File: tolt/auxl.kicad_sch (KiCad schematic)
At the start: 8 parts, among them U17 BMI160, U18 ESP32-C3_SUPERMINI_SMD

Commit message: modified:   tolt/auxl.kicad_sch 	modified:   tolt/converters.kicad_sch 	modified:   tolt/tolt.kicad_pcb
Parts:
- added C144: 100n, Capacitor_SMD:C_0402_1005Metric, symbol Device:C
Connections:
- net GND: now also C144.1
- net VCC: no longer U17.8 (VDD)
- new net VDDA: C144.2, U17.8 (VDD)
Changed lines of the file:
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@@
 	(wire
 		(pts
-			(xy 67.564 66.548) (xy 67.564 68.326)
+			(xy 67.564 66.04) (xy 67.564 68.326)
 		)
 		(stroke
@@
 	)
 	(symbol
+		(lib_id "power:VDDA")
+		(at 67.564 66.04 0)
+		(unit 1)
+		(exclude_from_sim no)
+		(in_bom yes)
+		(on_board yes)
+		(dnp no)
+		(fields_autoplaced yes)
+		(property "Reference" "#PWR057"
+			(at 67.564 69.85 0)
+			(effects
+				(font
+					(size 1.27 1.27)
+				)
+				(hide yes)
+			)
+		)
+		(property "Value" "VDDA"
+			(at 67.564 61.214 0)
+			(effects
+				(font
+					(size 1.27 1.27)
+				)
+			)
+		)
+		(property "Footprint" ""
+			(at 67.564 66.04 0)
+			(effects
+				(font
+					(size 1.27 1.27)
+				)
+				(hide yes)
+			)
+		)
+		(property "Datasheet" ""
+			(at 67.564 66.04 0)
+			(effects
+				(font
+					(size 1.27 1.27)
+				)
+				(hide yes)
+			)
+		)
+		(property "Description" ""
+			(at 67.564 66.04 0)
+			(effects
+				(font
+					(size 1.27 1.27)
+				)
+				(hide yes)
+			)
+		)
+		(pin "1"
+		)
+		(instances
+			(project "tolt"
+				(path "/38c63d96-01d7-4159-b7c0-aa8cee77c3e9/5e8c7753-d04d-42ed-8285-d224e0d20653"
+					(reference "#PWR057")
+					(unit 1)
+				)
+			)
+		)
+	)
+	(symbol
 		(lib_id "Device:C")
 		(at 57.404 32.258 180)
@@
 	)
 	(symbol
+		(lib_id "Device:C")
+		(at 69.342 32.004 180)
+		(unit 1)
+		(exclude_from_sim no)
+		(in_bom yes)
+		(on_board yes)
+		(dnp no)
+		(fields_autoplaced yes)
+		(property "Reference" "C144"
+			(at 72.644 30.734 0)
+			(effects
+				(font
+					(size 1.27 1.27)
+				)
+				(justify right)
+			)
+		)
+		(property "Value" "100n"
+			(at 72.644 33.274 0)
+			(effects
+				(font
+					(size 1.27 1.27)
+				)
+				(justify right)
+			)
+		)
+		(property "Footprint" "Capacitor_SMD:C_0402_1005Metric"
+			(at 68.3768 28.194 0)
+			(effects
+				(font
+					(size 1.27 1.27)
+				)
+				(hide yes)
+			)
+		)
+		(property "Datasheet" "~"
+			(at 69.342 32.004 0)
+			(effects
+				(font
+					(size 1.27 1.27)
+				)
+				(hide yes)
+			)
+		)
+		(property "Description" ""
+			(at 69.342 32.004 0)
+			(effects
+				(font
+					(size 1.27 1.27)
+				)
+				(hide yes)
+			)
+		)
+		(pin "1"
+		)
+		(pin "2"
+		)
+		(instances
+			(project "tolt"
+				(path "/38c63d96-01d7-4159-b7c0-aa8cee77c3e9/5e8c7753-d04d-42ed-8285-d224e0d20653"
+					(reference "C144")
+					(unit 1)
+				)
+			)
+		)
+	)
+	(symbol
 		(lib_id "power:VCC")
 		(at 65.024 68.326 0)
@@
 	)
 	(symbol
+		(lib_id "power:VDDA")
+		(at 69.342 28.194 0)
+		(unit 1)
+		(exclude_from_sim no)
+		(in_bom yes)
+		(on_board yes)
+		(dnp no)
+		(fields_autoplaced yes)
+		(property "Reference" "#PWR062"
+			(at 69.342 32.004 0)
+			(effects
+				(font
+					(size 1.27 1.27)
+				)
+				(hide yes)
+			)
+		)
+		(property "Value" "VDDA"
+			(at 69.342 23.368 0)
+			(effects
+				(font
+					(size 1.27 1.27)
+				)
+			)
+		)
+		(property "Footprint" ""
+			(at 69.342 28.194 0)
+			(effects
+				(font
+					(size 1.27 1.27)
+				)
+				(hide yes)
+			)
+		)
+		(property "Datasheet" ""
+			(at 69.342 28.194 0)
+			(effects
+				(font
+					(size 1.27 1.27)
+				)
+				(hide yes)
+			)
+		)
+		(property "Description" ""
+			(at 69.342 28.194 0)
+			(effects
+				(font
+					(size 1.27 1.27)
+				)
+				(hide yes)
+			)
+		)
+		(pin "1"
+		)
+		(instances
+			(project "tolt"
+				(path "/38c63d96-01d7-4159-b7c0-aa8cee77c3e9/5e8c7753-d04d-42ed-8285-d224e0d20653"
+					(reference "#PWR062")
+					(unit 1)
+				)
+			)
+		)
+	)
+	(symbol
 		(lib_id "power:VCC")
 		(at 47.498 70.866 0)
@@
 	(symbol
 		(lib_id "power:VCC")
-		(at 67.564 66.548 0)
-		(unit 1)
-		(exclude_from_sim no)
-		(in_bom yes)
-		(on_board yes)
-		(dnp no)
-		(fields_autoplaced yes)
-		(property "Reference" "#PWR0172"
-			(at 67.564 70.358 0)
-			(effects
-				(font
-					(size 1.27 1.27)
-				)
-				(hide yes)
-			)
-		)
-		(property "Value" "VCC"
-			(at 67.564 61.468 0)
-			(effects
-				(font
-					(size 1.27 1.27)
-				)
-			)
-		)
-		(property "Footprint" ""
-			(at 67.564 66.548 0)
-			(effects
-				(font
-					(size 1.27 1.27)
-				)
-				(hide yes)
-			)
-		)
-		(property "Datasheet" ""
-			(at 67.564 66.548 0)
-			(effects
-				(font
-					(size 1.27 1.27)
-				)
-				(hide yes)
-			)
-		)
-		(property "Description" "Power symbol creates a global label with name \"VCC\""
-			(at 67.564 66.548 0)
-			(effects
-				(font
-					(size 1.27 1.27)
-				)
-				(hide yes)
-			)
-		)
-		(pin "1"
-		)
-		(instances
-			(project "tolt"
-				(path "/38c63d96-01d7-4159-b7c0-aa8cee77c3e9/5e8c7753-d04d-42ed-8285-d224e0d20653"
-					(reference "#PWR0172")
-					(unit 1)
-				)
-			)
-		)
-	)
-	(symbol
-		(lib_id "power:VCC")
 		(at 57.404 28.448 0)
 		(unit 1)
@@
 					(unit 1)
 				)
+			)
+		)
+	)
+	(symbol
+		(lib_id "power:GND")
+		(at 69.342 35.814 0)
+		(unit 1)
+		(exclude_from_sim no)
+		(in_bom yes)
+		(on_board yes)
+		(dnp no)
+		(fields_autoplaced yes)
+		(property "Reference" "#PWR061"
+			(at 69.342 42.164 0)
+			(effects
+				(font
+					(size 1.27 1.27)
+				)
+				(hide yes)
+			)
+		)
+		(property "Value" "GND"
+			(at 69.342 40.894 0)
+			(effects
+				(font
+					(size 1.27 1.27)
+				)
+			)
+		)
+		(property "Footprint" ""
+			(at 69.342 35.814 0)
+			(effects
+				(font
+					(size 1.27 1.27)
+				)
+				(hide yes)
+			)
+		)
+		(property "Datasheet" ""
+			(at 69.342 35.814 0)
+			(effects
+				(font
+					(size 1.27 1.27)
+				)
+				(hide yes)
+			)
+		)
+		(property "Description" ""
+			(at 69.342 35.814 0)
+			(effects
+				(font
+					(size 1.27 1.27)
+				)
+				(hide yes)
+			)
+		)
+		(pin "1"
+		)
+		(instances
+			(project "tolt"
+				(path "/38c63d96-01d7-4159-b7c0-aa8cee77c3e9/5e8c7753-d04d-42ed-8285-d224e0d20653"
+					(reference "#PWR061")
+					(unit 1)
+				)

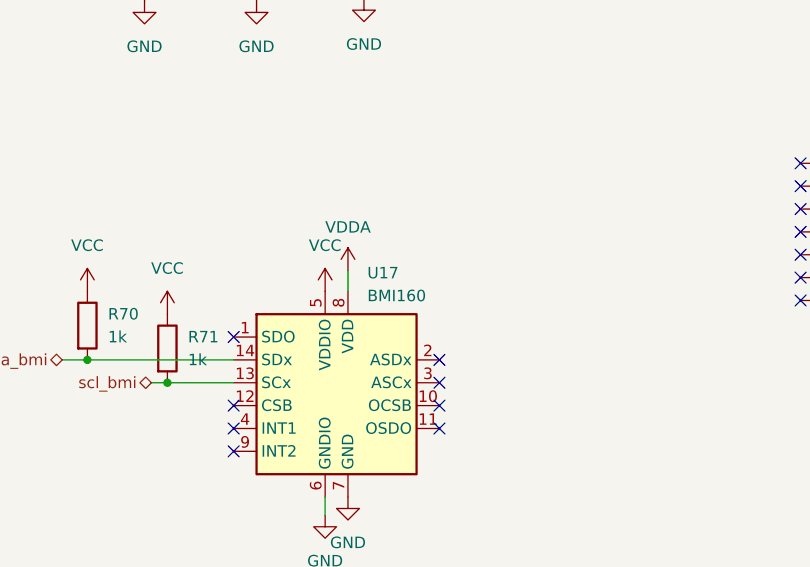
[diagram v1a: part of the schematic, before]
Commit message: more assign+12-5v change
changed with TPS82130
Since using esp32 will increase consumption by a lot
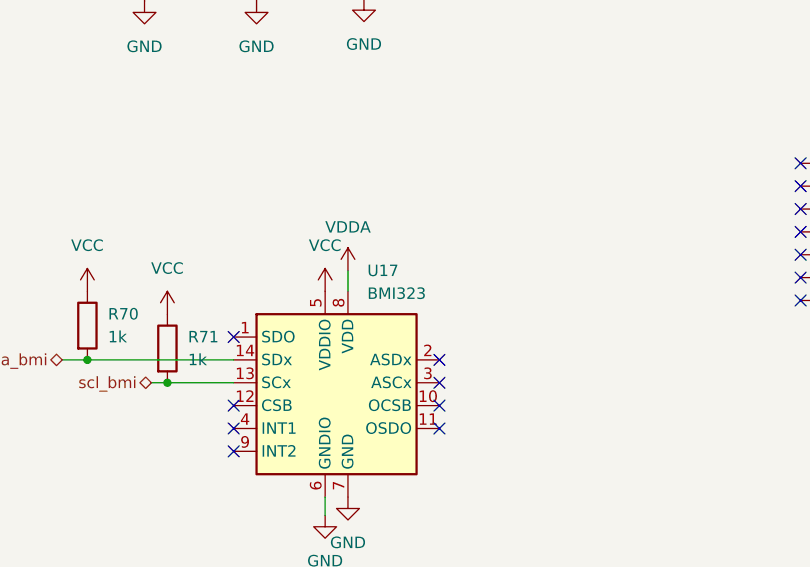
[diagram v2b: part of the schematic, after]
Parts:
- R70, R71: LCSC (none) -> C2907114
- U17: value BMI160 -> BMI323; LCSC (none) -> C5368700
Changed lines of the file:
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@@
+			)
+		)
+		(property "LCSC" "C2907114"
+			(at 38.608 72.136 0)
+			(effects
+				(font
+					(size 1.27 1.27)
+				)
+				(hide yes)
 			)
 		)
@@
 		(fields_autoplaced yes)
 		(property "Reference" "U17"
-			(at 69.7073 66.294 0)
+			(at 69.7073 66.04 0)
 			(effects
 				(font
@@
 			)
 		)
-		(property "Value" "BMI160"
-			(at 69.7073 68.834 0)
+		(property "Value" "BMI323"
+			(at 69.7073 68.58 0)
 			(effects
 				(font
@@
 		)
 		(property "Description" "Small, low power inertial measurement unit, LGA-14"
+			(at 67.564 78.486 0)
+			(effects
+				(font
+					(size 1.27 1.27)
+				)
+				(hide yes)
+			)
+		)
+		(property "LCSC" "C5368700"
 			(at 67.564 78.486 0)
 			(effects
@@
 			(at 47.498 74.676 0)
 			(effects
+				(font
+					(size 1.27 1.27)
+				)
+				(hide yes)
+			)
+		)
+		(property "LCSC" "C2907114"
+			(at 47.498 74.676 0)
+			(effects

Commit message: hm
weird huh it didnt fucking save
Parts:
- C144, C79: LCSC (none) -> C60474
- C78: LCSC (none) -> C913904
- C83, C84: LCSC (none) -> C98192
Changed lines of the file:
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@@
+			)
+		)
+		(property "LCSC" "C98192"
+			(at 171.704 50.546 0)
+			(effects
+				(font
+					(size 1.27 1.27)
+				)
+				(hide yes)
 			)
 		)
@@
 			)
 		)
+		(property "LCSC" "C60474"
+			(at 57.404 32.258 0)
+			(effects
+				(font
+					(size 1.27 1.27)
+				)
+				(hide yes)
+			)
+		)
 		(pin "1"
 		)
@@
 			)
 		)
+		(property "LCSC" "C913904"
+			(at 44.958 32.258 0)
+			(effects
+				(font
+					(size 1.27 1.27)
+				)
+				(hide yes)
+			)
+		)
 		(pin "1"
 		)
@@
 			)
 		)
+		(property "LCSC" "C60474"
+			(at 69.342 32.004 0)
+			(effects
+				(font
+					(size 1.27 1.27)
+				)
+				(hide yes)
+			)
+		)
 		(pin "1"
 		)
@@
 			(at 166.37 50.546 0)
 			(effects
+				(font
+					(size 1.27 1.27)
+				)
+				(hide yes)
+			)
+		)
+		(property "LCSC" "C98192"
+			(at 166.37 50.546 0)
+			(effects

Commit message: fab
finally.
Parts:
- C78: value 2.2u -> 2.2uf
- R70, R71: LCSC C2907114 -> C22548
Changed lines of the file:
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@@
 			)
 		)
-		(property "Value" "2.2u"
+		(property "Value" "2.2uf"
 			(at 48.768 33.528 0)
 			(effects
@@
 			)
 		)
-		(property "LCSC" "C2907114"
+		(property "LCSC" "C22548"
 			(at 38.608 72.136 0)
 			(effects
@@
 			)
 		)
-		(property "LCSC" "C2907114"
+		(property "LCSC" "C22548"
 			(at 47.498 74.676 0)
 			(effects
